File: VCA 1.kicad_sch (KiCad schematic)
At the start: 64 parts, among them J1 Eurorack 2x8hs, J15 IN 1x8s, J2 OUT 1x3s, J3 CV 1x9s, Q1 2N3904, Q2 2N3904, U1 TL074, U2 AS2164

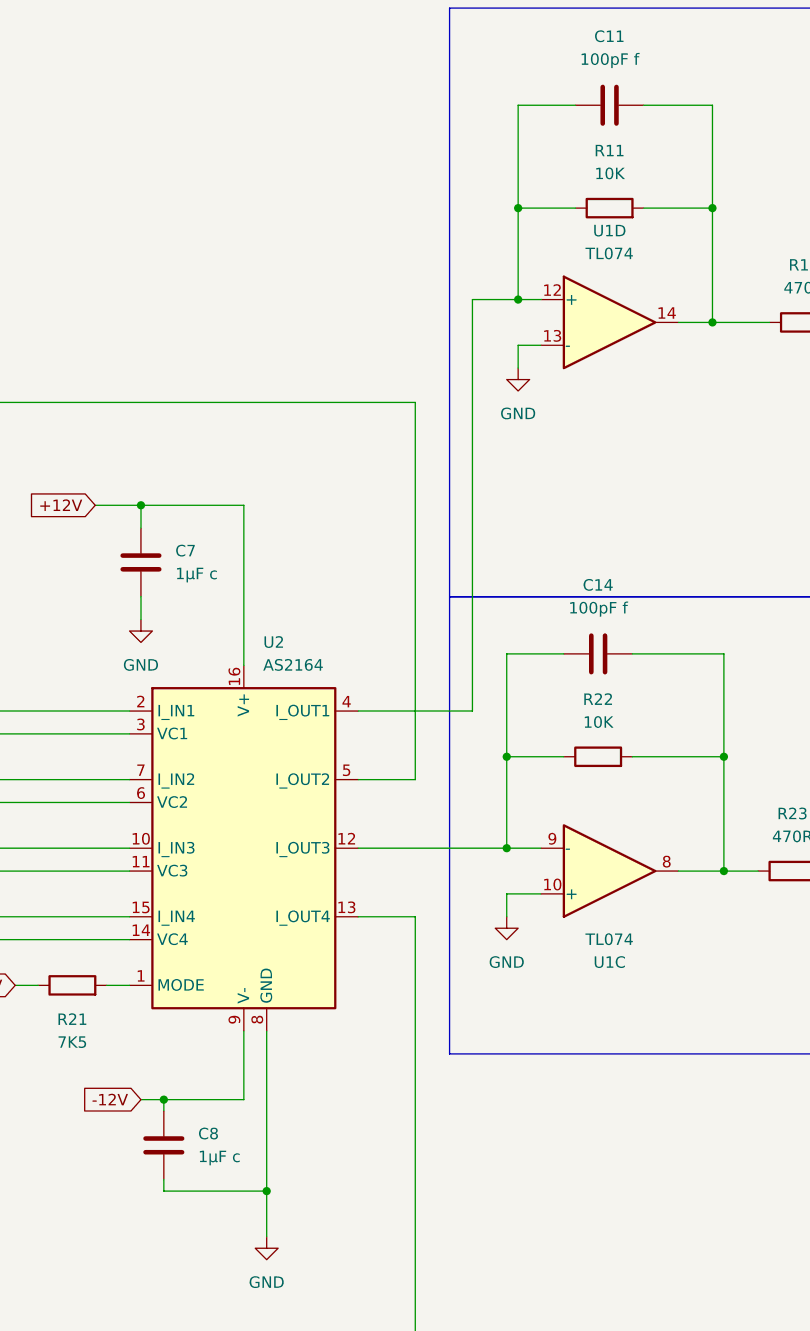
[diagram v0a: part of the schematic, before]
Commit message: Forgot panel pins are soldered on reverse
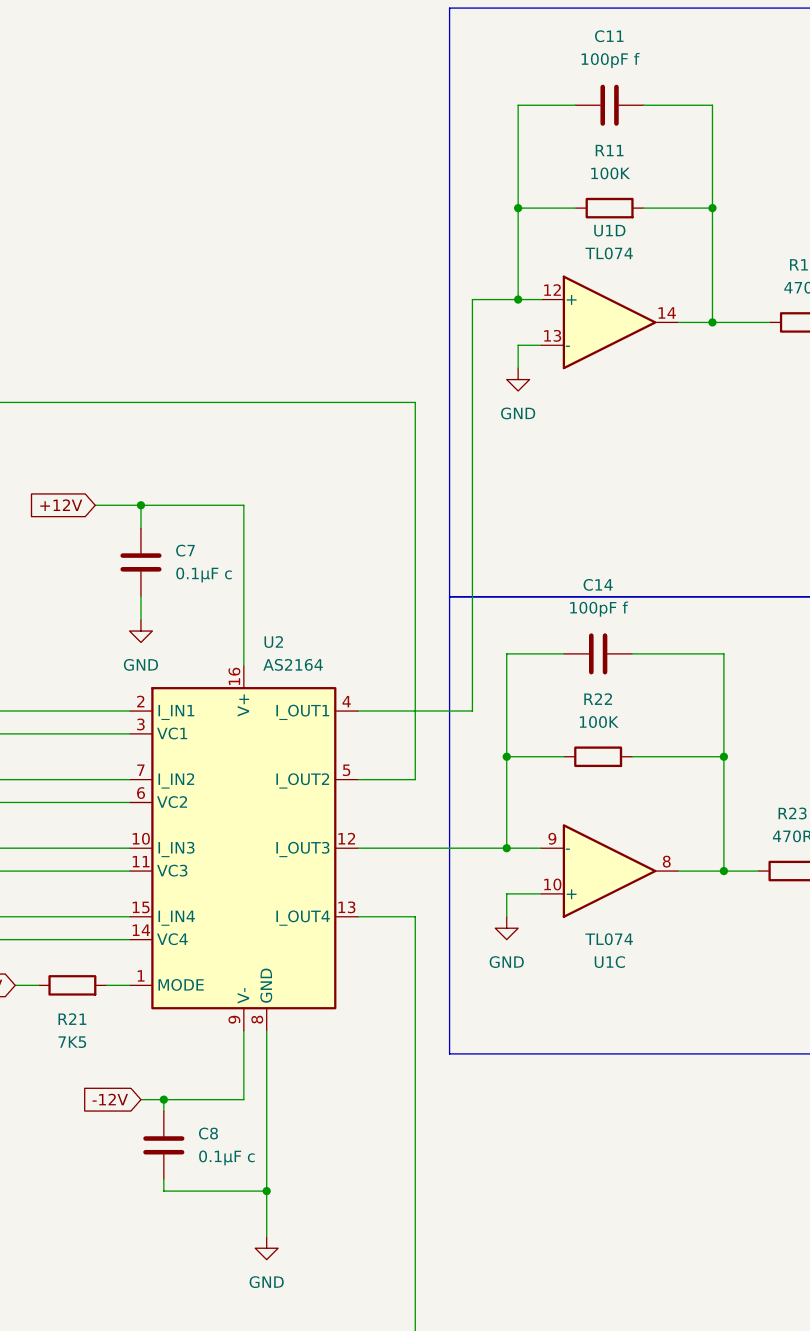
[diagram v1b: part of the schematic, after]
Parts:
- C7, C8: value 1μF c -> 0.1μF c
- R11, R22: value 10K -> 100K
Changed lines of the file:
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@@
 			)
 		)
-		(property "Value" "10K"
+		(property "Value" "100K"
 			(at 232.41 35.56 90)
 			(show_name no)
@@
 			)
 		)
-		(property "Value" "1μF c"
+		(property "Value" "0.1μF c"
 			(at 186.69 144.7799 0)
 			(show_name no)
@@
 			)
 		)
-		(property "Value" "1μF c"
+		(property "Value" "0.1μF c"
 			(at 184.15 80.0099 0)
 			(show_name no)
@@
 			)
 		)
-		(property "Value" "10K"
+		(property "Value" "100K"
 			(at 231.14 96.52 90)
 			(show_name no)

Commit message: Updated versioning
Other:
- note added: "V 1.0"
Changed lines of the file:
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@@
+		)
+	)
+	(text "V 1.0"
+		(exclude_from_sim no)
+		(at 394.462 280.162 0)
+		(effects
+			(font
+				(size 1.27 1.27)
+			)
 		)
 	)

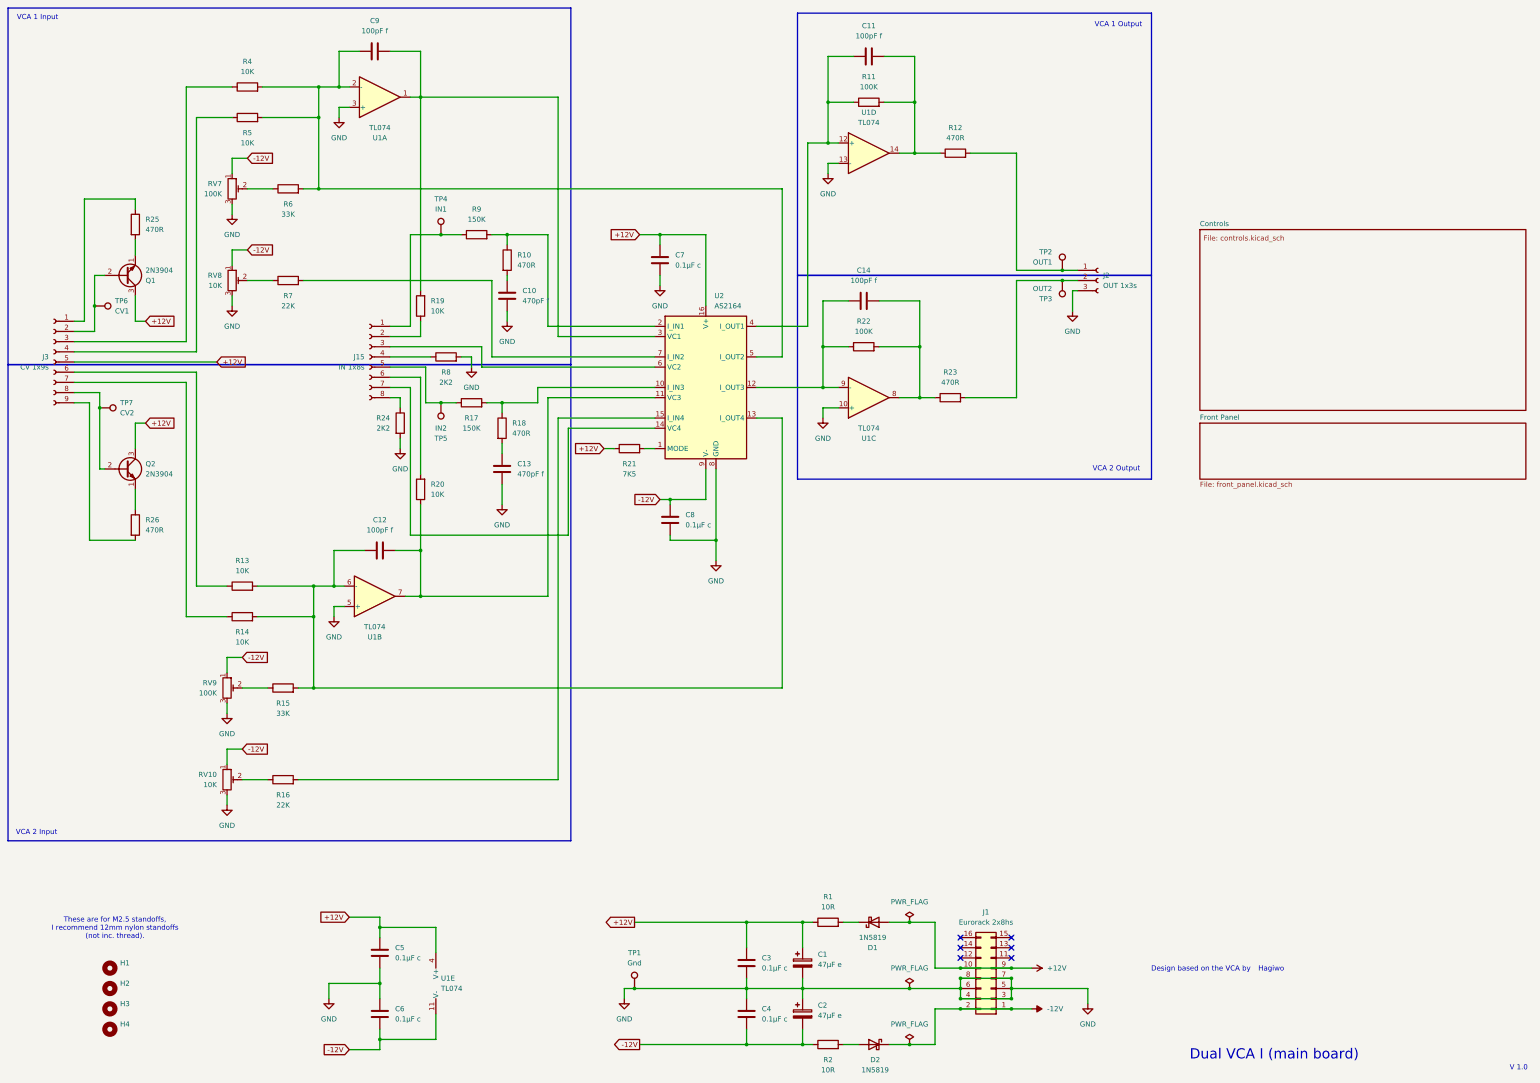
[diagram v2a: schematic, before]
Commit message: Reoriented power and fixed flags
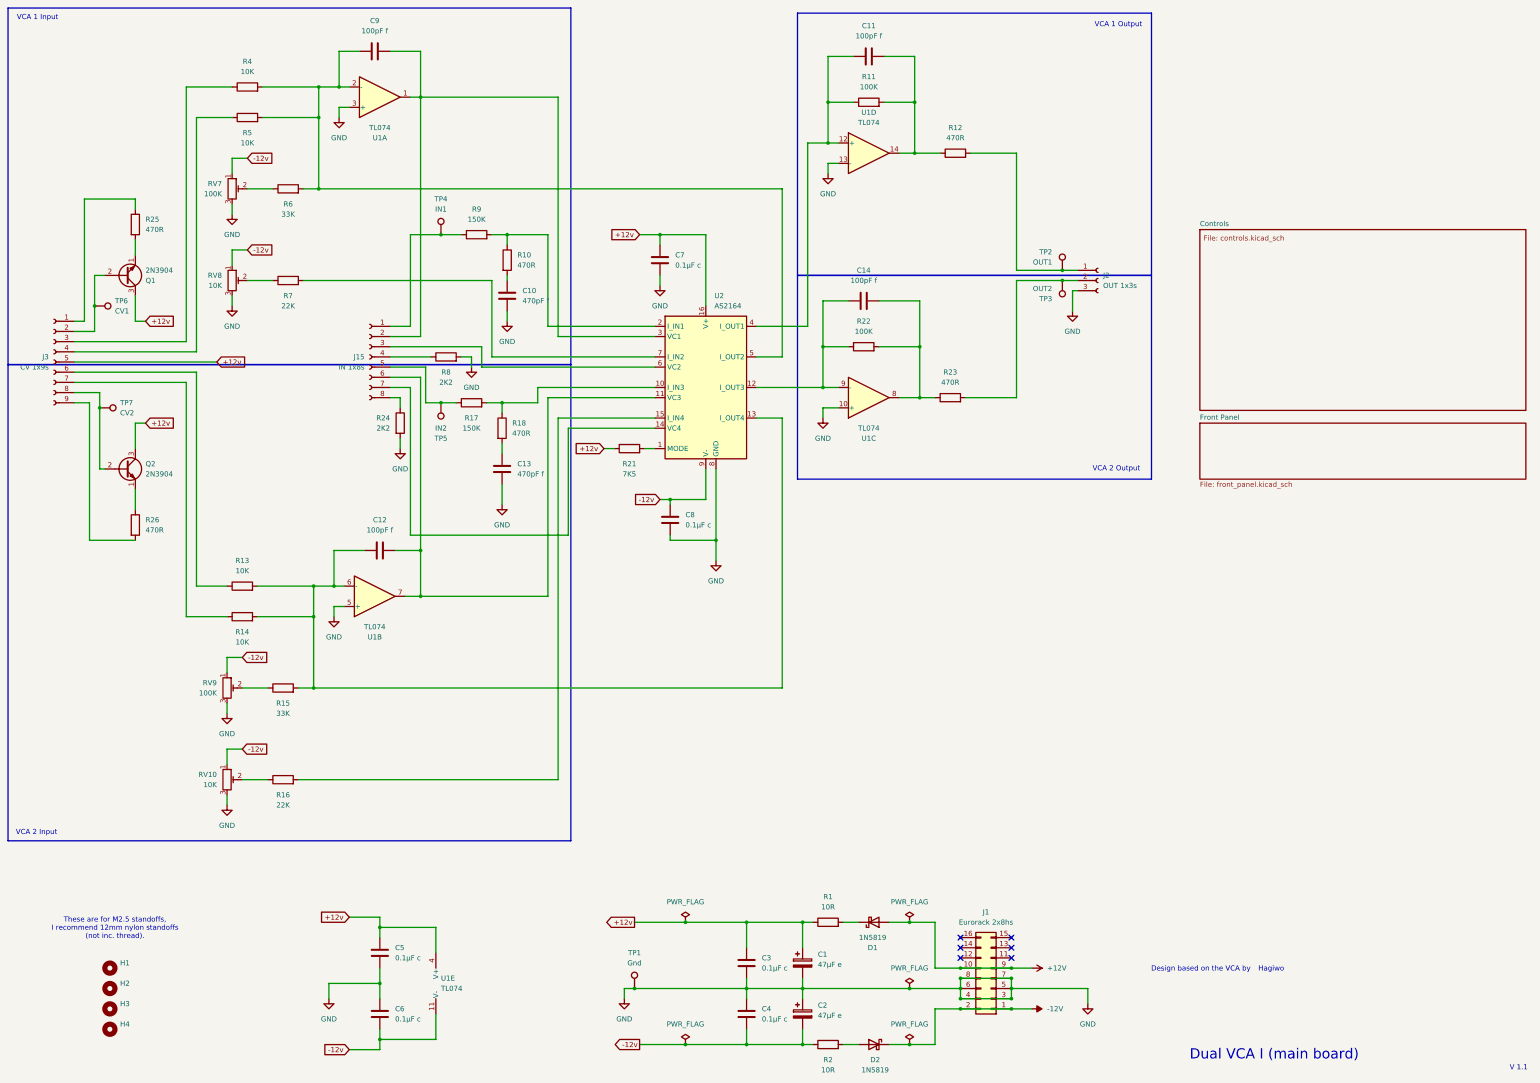
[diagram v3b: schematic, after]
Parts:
- removed R19: 10K, Resistor_THT:R_Axial_DIN0204_L3.6mm_D1.6mm_P2.54mm_Vertical, symbol Device:R
- removed R20: 10K, Resistor_THT:R_Axial_DIN0204_L3.6mm_D1.6mm_P7.62mm_Horizontal, symbol Device:R
- R21: footprint Resistor_THT:R_Axial_DIN0204_L3.6mm_D1.6mm_P2.54mm_Vertical -> Resistor_THT:R_Axial_DIN0204_L3.6mm_D1.6mm_P7.62mm_Horizontal
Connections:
- net +12V: no longer C1.1, C3.1, C5.1, C7.1, J3.5 (Pin_5), Q1.3 (C), Q2.3 (C), R1.1, R21.1, U1.4 (V+), U2.16 (V+)
- net -12V: no longer C2.2, C4.2, C6.2, C8.1, R2.1, RV10.1, RV7.1, RV8.1, RV9.1, U1.11 (V-), U2.9 (V-)
- net at C9.2, U1.1, U2.3 (VC1): now also J15.2 (Pin_2)
- net at C12.2, U1.7, U2.11 (VC3): now also J15.6 (Pin_6)
- new net +12v: C1.1, C3.1, C5.1, C7.1, J3.5 (Pin_5), Q1.3 (C), Q2.3 (C), R1.1, R21.1, U1.4 (V+), U2.16 (V+)
- new net -12v: C2.2, C4.2, C6.2, C8.1, R2.1, RV10.1, RV7.1, RV8.1, RV9.1, U1.11 (V-), U2.9 (V-)
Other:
- note added: "V 1.1"
- note removed: "V 1.0"
